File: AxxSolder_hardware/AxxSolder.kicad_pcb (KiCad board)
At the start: 2 copper layers, 39 x 82.5 mm, 138 parts, among them IC1 TLV76733DRVR, IC2 OPA2387DSGT, IC3 LMR54406DBVR, IC4 STM32G431CBT6, IC5 TPD4E1U06DBVR, IC6 STUSB4500QTR, IC7 MAX16171ATA_VY+T, IC8 LTC4440AHMS8E, IC9 INA281A5QDBVRQ1, J1 USB4110-GF-A, J2 691243110009, J3 TSW-102-07-T-S, J4 61300611821, J5 TSW-102-07-T-S, J6 TSW-102-07-T-S, Q1 STL9P3LLH6, Q2 STL10N3LLH5, Q3 2N7002NXAKR, U2 PEC11J-9215F-S0015, U3 BSC014N04LS

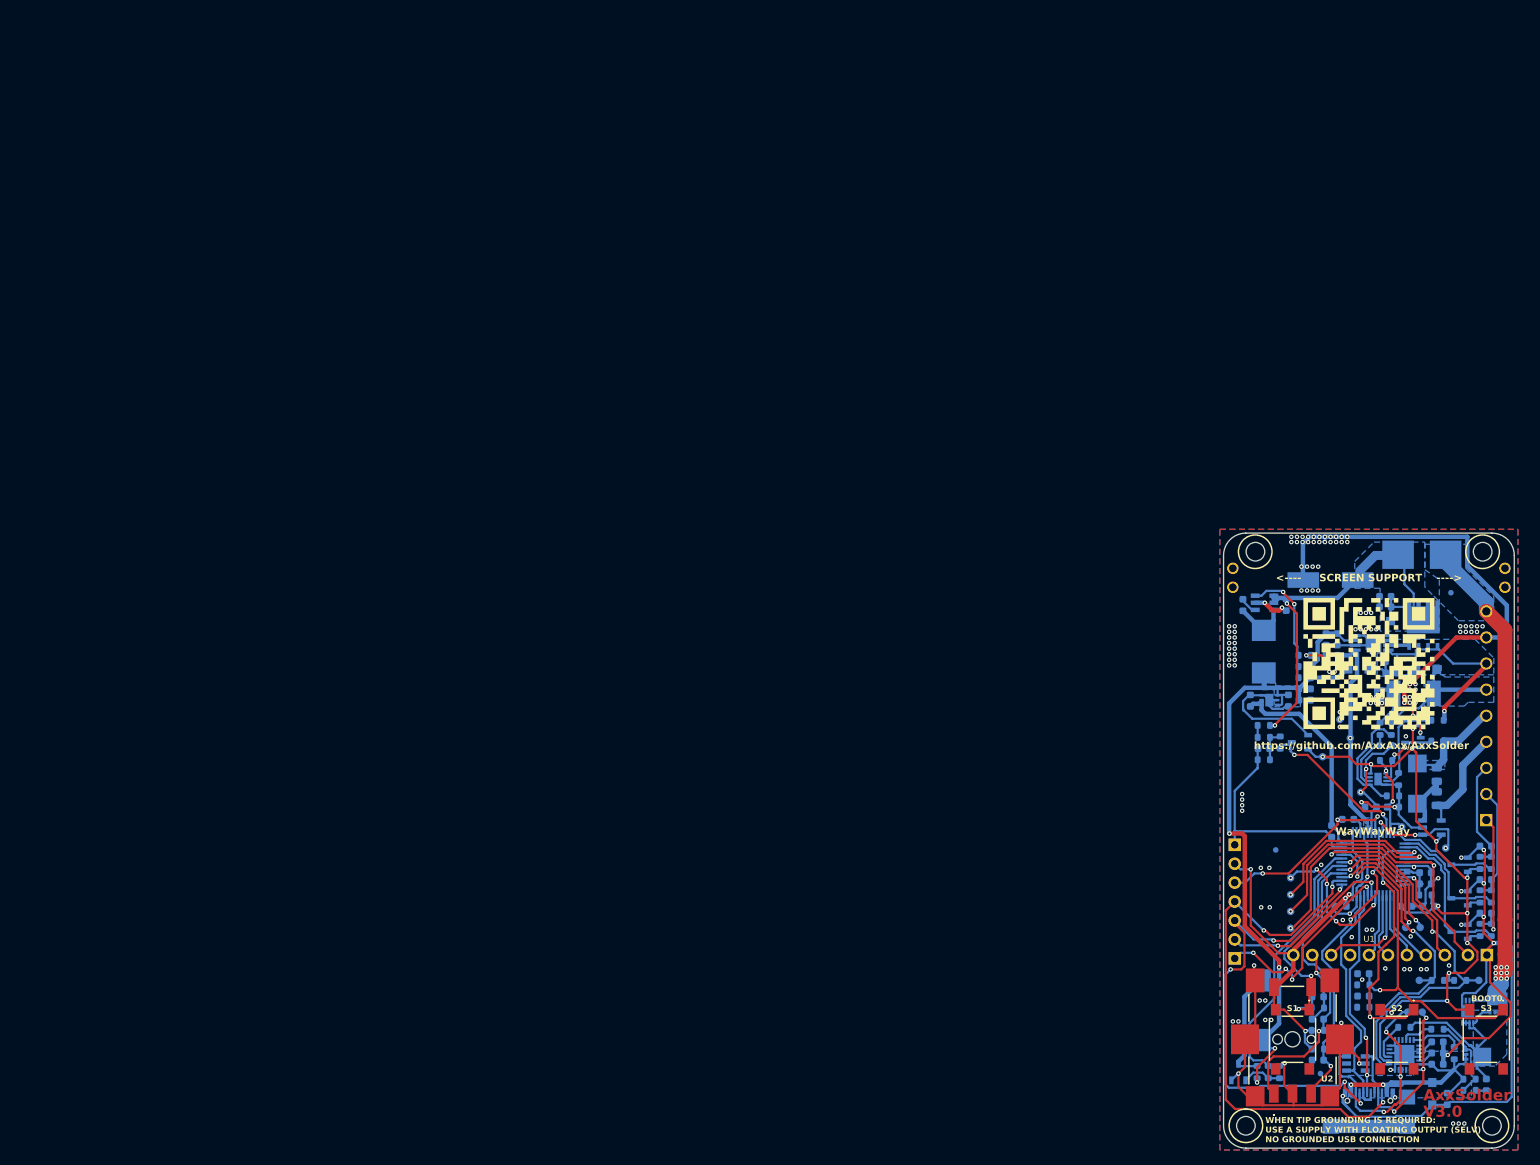
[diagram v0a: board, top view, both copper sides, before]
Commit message: Replace MCU with RP2040, new PCB layout
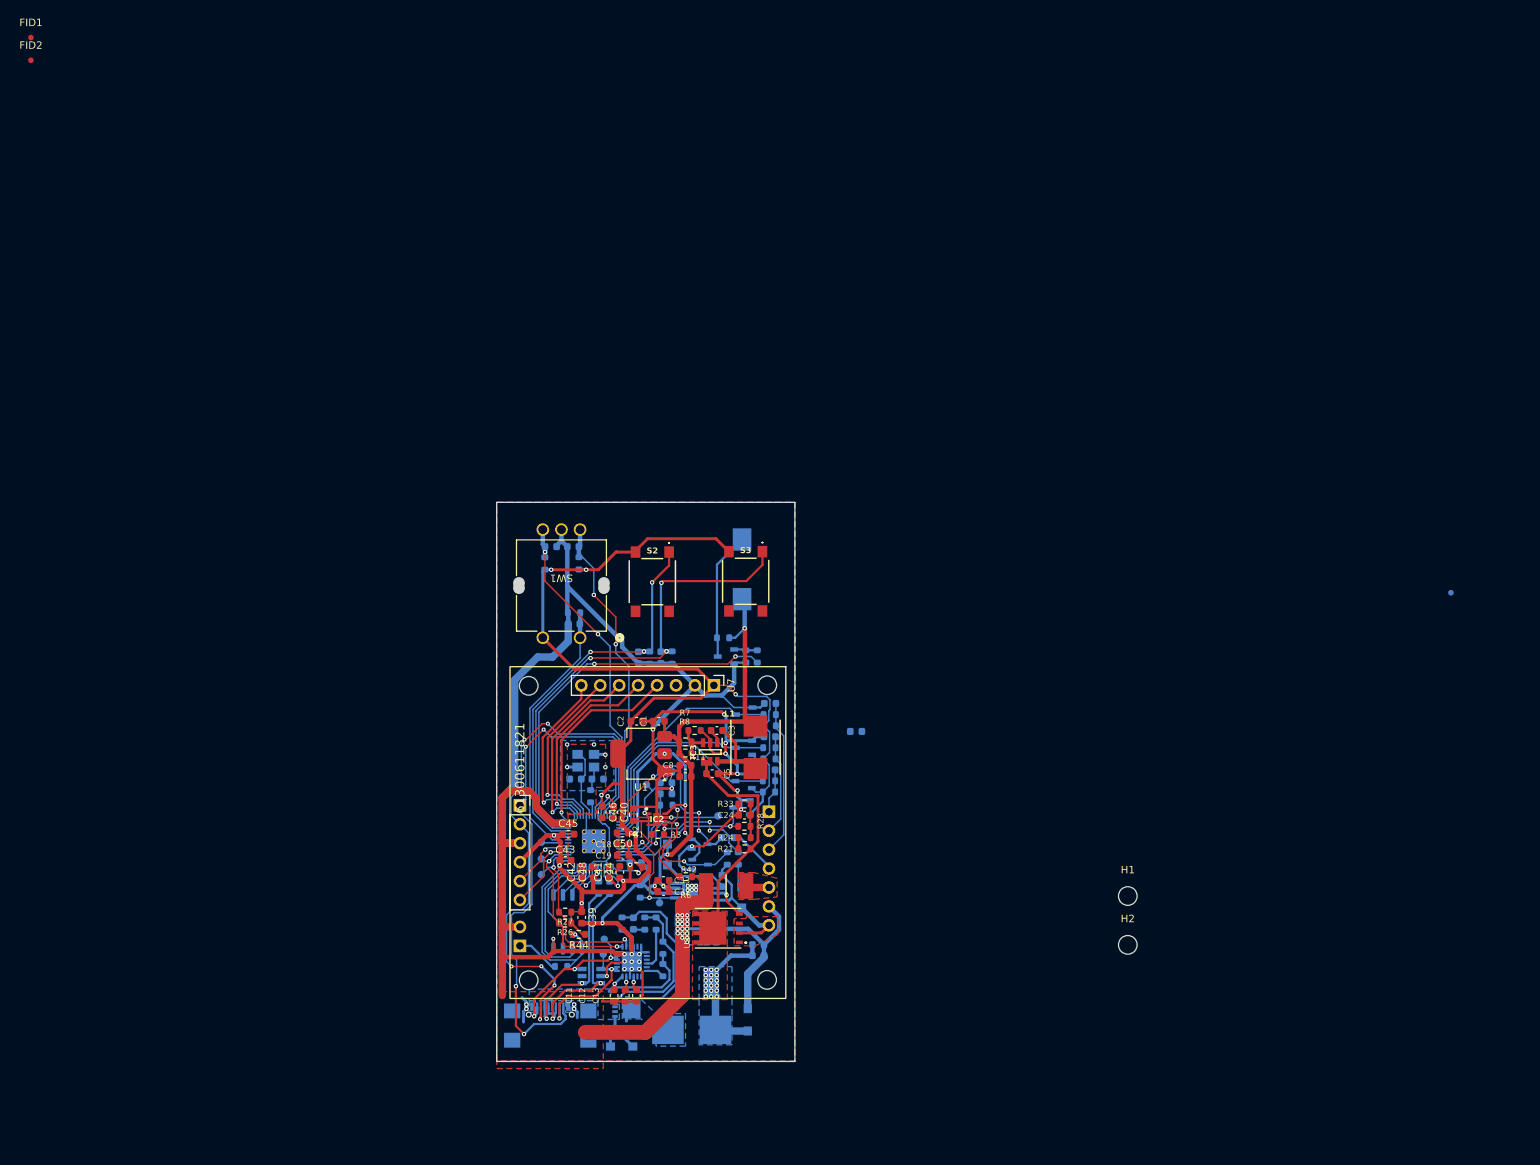
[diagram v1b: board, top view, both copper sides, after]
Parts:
- removed C14, C15, C16, C17: 100n, Capacitor_SMD:C_0603_1608Metric
- removed C31: 10u, Capacitor_SMD:C_0603_1608Metric
- removed F2: SF-2410FP100W-2, footprints:SF2410FP100W2
- removed G***: LOGO, LOGO
- removed IC1: TLV76733DRVR, footprints:SON65P200X200X80-7N
- removed IC4: STM32G431CBT6, footprints:QFP50P900X900X160-48N
- removed IC7: MAX16171ATA_VY+T, footprints:SON50P300X200X80-9N
- removed IC9: INA281A5QDBVRQ1, footprints:SOT95P280X145-5N
- removed J3: TSW-102-07-T-S, Connector_PinHeader_2.54mm:PinHeader_1x02_P2.54mm_Vertical
- removed J5, J6: TSW-102-07-T-S, footprints:TSW-102-XX-YY-S
- removed Q2: STL10N3LLH5, footprints:STL10N3LLH5
- removed S1: ADTSM644RVTR, footprints:ADTSM644RVTR
- removed TP1, TP14, TP2, TP5, TP6: DIAG_TP, TestPoint:TestPoint_Pad_D1.0mm
- removed TP12: GND_TP, TestPoint:TestPoint_Pad_D1.0mm
- removed TP13: DIAG_TP, Connector_PinSocket_2.54mm:PinSocket_1x01_P2.54mm_Vertical
- removed TP3: 3.3V_TP, TestPoint:TestPoint_Pad_D1.0mm
- removed TP9: Current_TP, TestPoint:TestPoint_Pad_D1.0mm
- removed U2: PEC11J-9215F-S0015, footprints:PEC11J9215FS0015
- added C36: 15p, Capacitor_SMD:C_0603_1608Metric, B.Cu at (74.1, 100.5)
- added C38: 15p, Capacitor_SMD:C_0603_1608Metric, B.Cu at (77.1, 100.5)
- added C39: 100n, Capacitor_SMD:C_0603_1608Metric, F.Cu at (74.9, 119.0)
- added C40: 100n, Capacitor_SMD:C_0603_1608Metric, F.Cu at (79.2, 104.9)
- added C41: 100n, Capacitor_SMD:C_0603_1608Metric, F.Cu at (78.5, 113.0)
- added C42: 1u, Capacitor_SMD:C_0603_1608Metric, F.Cu at (74.9, 113.0)
- added C43: 100n, Capacitor_SMD:C_0603_1608Metric, F.Cu at (72.7, 111.4)
- added C44: 1u, Capacitor_SMD:C_0603_1608Metric, F.Cu at (80.0, 113.0)
- added C45: 100n, Capacitor_SMD:C_0603_1608Metric, F.Cu at (73.1, 107.9)
- added C46: 100n, Capacitor_SMD:C_0603_1608Metric, F.Cu at (77.6, 104.9)
- added C47: 100n, Capacitor_SMD:C_0603_1608Metric, B.Cu at (82.1, 111.7)
- added C48: 100n, Capacitor_SMD:C_0603_1608Metric, F.Cu at (76.5, 113.0)
- added C50: 100n, Capacitor_SMD:C_0603_1608Metric, F.Cu at (80.4, 107.7)
- added H3: MountingHole, MountingHole:MountingHole_2.5mm, F.Cu at (67.8, 88.0)
- added H4: MountingHole, MountingHole:MountingHole_2.5mm, F.Cu at (99.8, 87.9)
- added H5: MountingHole, MountingHole:MountingHole_2.5mm, F.Cu at (67.8, 127.5)
- added H6: MountingHole, MountingHole:MountingHole_2.5mm, F.Cu at (99.8, 127.4)
- added J7: Conn_01x07_Pin, Connector_PinHeader_2.54mm:PinHeader_1x07_P2.54mm_Vertical, B.Cu at (100.0, 104.9)
- added R16: 1k, Resistor_SMD:R_0603_1608Metric, B.Cu at (76.1, 102.8)
- added R43: 1k, Resistor_SMD:R_0603_1608Metric, B.Cu at (72.1, 125.6)
- added R46: 27, Resistor_SMD:R_0603_1608Metric, B.Cu at (78.7, 115.1)
- added SW1: PEC11L-4220F-S0015, custom:PEC11L-4xxxF-Sxxxx_BRN, F.Cu at (74.7, 81.5)
- added U5: RP2040, custom:RP2040-QFN-56, B.Cu at (76.5, 108.8)
- added U6: W25Q128JVS, Package_SO:SOIC-8_5.23x5.23mm_P1.27mm, B.Cu at (73.0, 119.6)
- added U7: WS3-013992, custom:WS-13992, F.Cu at (92.6, 87.9)
- added Y1: ABM8-272-T3, Crystal:Crystal_SMD_3225-4Pin_3.2x2.5mm, B.Cu at (75.5, 98.0)
- C1, C11, C12, C13, C18, C19, C2, C24, C3, C32, C33, C5, C7, C8, FB1, FID1, FID2, IC2, IC3, J4, L1, R11, R2, R21, R24, R26, R27, R28, R3, R33, R42, R6, R7, R8, U3: moved to F.Cu
- J2: value 691243110009 -> Conn_01x02; footprint footprints:691243110009 -> Connector_PinHeader_2.54mm:PinHeader_1x02_P2.54mm_Vertical
- R44: value 1M -> 10k; footprint Resistor_SMD:R_0805_2012Metric -> Resistor_SMD:R_0603_1608Metric; moved to F.Cu
- R45: value 100m -> 27; footprint Resistor_SMD:R_0805_2012Metric -> Resistor_SMD:R_0603_1608Metric
- U1: value ~ -> LD1117S33TR_SOT223; footprint footprints:Adafruit_240x320_TFT -> Package_TO_SOT_SMD:SOT-223-3_TabPin2
- moved FID2 220.0 mm to (1.02, 4.08), turned to 0 degrees
- moved FID1 199.4 mm to (1.02, 1.02), turned to 0 degrees
- moved J2 130.7 mm to (66.6, 122.9), turned to 0 degrees
- moved TP16 126.6 mm to (69.5, 113.3), turned to 90 degrees
- moved C29 123.8 mm to (70.8, 69.3), turned to 0 degrees
- moved R36 122.4 mm to (70.0, 71.6), turned to 90 degrees
- moved R27 120.4 mm to (72.7, 118.3), turned to 0 degrees
- moved TP15 118.9 mm to (69.5, 111.2), turned to 90 degrees
- moved C28 118.3 mm to (73.7, 69.3)
- moved R26 117.3 mm to (72.7, 119.8)
- moved R35 117.3 mm to (74.5, 71.6), turned to 90 degrees
- moved S2 117.2 mm to (84.4, 74.0)
- moved R44 117.1 mm to (74.5, 121.3), turned to 180 degrees
- moved F1 116.9 mm to (89.7, 134.1)
- moved S3 116.8 mm to (96.9, 74.0)
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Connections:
- C9 pad 2: /VDD_IN_USBCPD -> /VDD_IN
- F1 pad 1: VDD -> /VDD_IN
- F1 pad 2: /VDD_IN -> VDD
- J2 pad 1: /S_sense -> /~{USB_BOOT}
- J2 pad 2: /H_sense2 -> GND
- J4 pad 1: GND -> /SWCLK
- J4 pad 2: +3.3V -> /SWDIO
- J4 pad 3: /NRST -> GND
- J4 pad 4: /SWCLK -> +3.3V
- J4 pad 5: /SWDIO -> /USART_RX
- Q1 pad 5: /VDD_IN_USBCPD -> /VDD_IN
- R17 pad 2: /VDD_IN_USBCPD -> /VDD_IN
- R35 pad 1: /ENC_B -> +3.3V
- R35 pad 2: +3.3V -> /ENC_B
- R44 pad 1: Net-(IC9-IN+) -> +3.3V
- R44 pad 2: /GREEN -> /QSPI_SS
- R45 pad 1: Earth -> /USB_D+
- R45 pad 2: Net-(IC9-IN+) -> Net-(U5-USB_DP)
- U1 pad 3: GND -> +7.5V
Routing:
- net GND: track 447.9 -> 381.2 mm, vias 149 -> 55
- net /VDD_IN: track 70.6 -> 23.6 mm, vias 9 -> 0
- net /USR4: track 46.0 -> 0.00 mm, vias 2 -> 0
- net +7.5V: track 95.8 -> 64.6 mm, vias 4 -> 3
- net /SDA: track 52.6 -> 24.7 mm
- net /NRST: track 26.5 -> 0.00 mm, vias 3 -> 0
- net +3.3V: track 200.1 -> 226.5 mm, vias 16 -> 14
- net /USR3: track 26.1 -> 0.00 mm, vias 2 -> 0
- net /QSPI_SS: track 0.00 -> 25.3 mm, vias 0 -> 1
- net +1V1: track 0.00 -> 24.4 mm, vias 0 -> 3
- net /USR2: track 23.1 -> 0.00 mm, vias 2 -> 0
- net /VDD_IN_USBCPD: track 22.7 -> 0.00 mm
- net /USART_RX: track 29.0 -> 8.85 mm, vias 4 -> 1
- net /SW3: track 46.9 -> 66.7 mm, vias 2 -> 3
- net /QSPI_SD1: track 0.00 -> 19.2 mm
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- added copper zone on F.Cu, net /BLUE
- added copper zone on F.Cu, net /RED
- added copper zone on F.Cu, net VDD
- removed copper zone on B.Cu, net +7.5V
- removed copper zone on B.Cu, net /BLUE
- removed copper zone on B.Cu, net /BOOST
- removed copper zone on B.Cu, net /GREEN
- removed copper zone on B.Cu, net /Heater
- removed copper zone on B.Cu, net /RED
- removed copper zone on B.Cu, net /VDD_IN_USBCPD
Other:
- board size 39 x 82.5 mm -> 40 x 75 mm
- board text removed: "2024-02"
- board text removed: "3.3V"
- board text removed: "9-24 VDC"
- board text removed: "<---- SCREEN SUPPORT ---->"
- board text removed: "AxxAxx"
- board text removed: "AxxSolder"
- board text removed: "BLU"
- board text removed: "BOOT0"
- board text removed: "C"
- board text removed: "GND"
- board text removed: "GRN"
- board text removed: "IN1"
- board text removed: "IN2"
- board text removed: "IO1"
- board text removed: "IO2"
- board text removed: "IO3"
- board text removed: "IO4"
- board text removed: "Input Voltage"
- board text removed: "NEVER SOLDER ON LIVE CIRCUITS!"
- board text removed: "NRST"
- board text removed: "PWM"
- board text removed: "RED"
- board text removed: "RX"
- board text removed: "SCL"
- board text removed: "SDA"
- board text removed: "STAND"
- board text removed: "STM32"
- board text removed: "STUSB4500"
- board text removed: "SWCLK"
- board text removed: "SWD"
- board text removed: "SWDIO"
- board text removed: "T"
- board text removed: "TX"
- board text removed: "USBC-PD"
- board text removed: "V3.0"
- board text removed: "VIN"
- board text removed: "WHEN TIP GROUNDING IS REQUIRED: USE A SUPPLY WITH FLOATING OUTPUT (SELV) NO GROUNDED USB CONNECTION"
- board text removed: "WayWayWay"
- board text removed: "https://github.com/AxxAxx/AxxSolder"

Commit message: Cleanup
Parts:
- removed H1, H2: MountingHole, MountingHole:MountingHole_2.5mm
- PWM: renamed from TP17; value SW_TP -> PWM
- moved FID2 166.4 mm to (101.6, 136.7)
- moved FID3 107.0 mm to (85.0, 65.3)
- moved R43 4.44 mm to (67.7, 125.4)
- moved C34 1.08 mm to (97.8, 123.5), turned to -90 degrees
- moved C35 1.01 mm to (99.3, 123.5), turned to -90 degrees
- moved U3 1.00 mm to (90.2, 121.5)
- renumbered TP7 to CC1, TP8 to CC2, TP10 to CURRENT, TP15 to SCL, TP16 to SDA, TP11 to TC
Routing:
- net GND: track 381.2 -> 375.7 mm, vias 55 -> 58
- net /~{USB_BOOT}: track 5.83 -> 2.64 mm
- net Net-(IC8-TG): track 6.19 -> 7.20 mm
- net /VBUS: track 20.5 -> 19.7 mm
- net /QSPI_SS: track 25.3 -> 25.8 mm
- net +1V1: track 24.4 -> 24.9 mm
- net /SWDIO: track 74.4 -> 73.9 mm
- net VDD: track 47.0 -> 47.2 mm, vias 18 -> 30

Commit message: Cleanup
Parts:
- removed C20: 10u, Capacitor_SMD:C_0603_1608Metric
- removed H3, H4, H5, H6: MountingHole, MountingHole:MountingHole_2.5mm
- removed J7: Conn_01x07_Pin, Connector_PinHeader_2.54mm:PinHeader_1x07_P2.54mm_Vertical
- removed SW1: PEC11L-4220F-S0015, custom:PEC11L-4xxxF-Sxxxx_BRN
- removed TP4: DIAG_TP, TestPoint:TestPoint_Pad_D1.0mm
- removed U7: WS3-013992, custom:WS-13992
- added C14: 100n, Capacitor_SMD:C_0603_1608Metric, F.Cu at (76.1, 94.7)
- added D11: 1_5inch-rgb-oled-module_asm-1110, custom_hmi:1_5inch-rgb-oled-module_asm-1110, F.Cu at (83.0, 114.0)
- added FID4: OSHW symbol, Symbol:OSHW-Logo_5.7x6mm_Copper, B.Cu at (80.8, 133.7)
- added FID5: Kicad symbol, Symbol:KiCad-Logo_6mm_SilkScreen, B.Cu at (88.2, 124.0)
- added J3: USB4105-GF-A, custom_connectors:GCT_USB4105-GF-A, F.Cu at (73.0, 62.7)
- added U2: PEC11L-4220F-S0015, custom_hmi:PEC11L4220FS0015, F.Cu at (71.6, 127.6)
- C10, C25, C26, C27, C4, C47, C6, C9, D1, D2, D3, D5, D6, D8, Q1, R1, R10, R12, R13, R14, R15, R17, R18, R19, R20, R22, R25, R29, R5, R9: moved to F.Cu
- C24, C3, C32, C33, C5, C7, C8, IC3, L1, R11, R21, R24, R26, R27, R28, R33, R42, R44, R7, R8, U3: moved to B.Cu
- J1: value USB4110-GF-A -> 284391-7; footprint footprints:USB4110GFA -> custom_connectors:CONN7_284391-7_TEC
- J4: footprint footprints:RHDR6W97P0X254_1X6_1574X250X865P -> Connector_PinHeader_2.54mm:PinHeader_1x06_P2.54mm_Vertical; moved to B.Cu
- TP10: renamed from CURRENT; value Current_TP -> Current
- TP11: renamed from TC; value TC_TP -> TC
- TP15: renamed from SCL; value DIAG_TP -> SCL
- TP16: renamed from SDA; value DIAG_TP -> SDA
- TP7: renamed from CC1; value DIAG_TP -> CC1
- TP8: renamed from CC2; value DIAG_TP -> CC2
- moved D3 74.3 mm to (66.7, 63.3), turned to 90 degrees
- moved FID3 70.4 mm to (85.2, 135.7)
- moved F1 68.9 mm to (84.0, 65.5)
- moved Q1 66.3 mm to (81.0, 65.1), turned to -90 degrees
- moved C28 63.3 mm to (69.9, 132.6), turned to 0 degrees
- moved C29 63.3 mm to (73.2, 132.6), turned to 180 degrees
- moved C10 63.0 mm to (74.0, 71.7), turned to 90 degrees
- moved D4 61.4 mm to (94.3, 71.5), turned to 0 degrees
- moved R35 59.7 mm to (69.9, 131.1), turned to 180 degrees
- moved R36 59.6 mm to (73.2, 131.1), turned to 0 degrees
- moved C37 58.9 mm to (96.7, 65.5), turned to 0 degrees
- moved C11 58.4 mm to (77.5, 71.2), turned to 0 degrees
- moved LS1 58.3 mm to (96.6, 130.4)
- moved C12 57.0 mm to (77.5, 72.7), turned to 0 degrees
- moved C13 55.6 mm to (77.5, 74.2), turned to 0 degrees
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- renumbered PWM to TP17
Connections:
- C28 pad 1: /ENC_B -> /ENC_A
- C29 pad 1: /ENC_A -> /ENC_B
- IC5 pad 3: /USB_D- -> /USB_D+
- IC5 pad 4: /USB_D+ -> /USB_D-
- R35 pad 2: /ENC_B -> /ENC_A
- R36 pad 2: /ENC_A -> /ENC_B
- U5 pad 11: /SW2 -> unconnected-(U5-GPIO8-Pad11)
- U5 pad 12: /SW3 -> /SW1
- U5 pad 13: /Buzzer -> /ENC_A
- U5 pad 14: /SPI_MOSI -> /SPI_RST
- U5 pad 15: /SPI_CS -> /SPI_DC
- U5 pad 16: /SPI_SCK -> /SPI_CS
- U5 pad 17: /SPI_RST -> /SPI_SCK
- U5 pad 18: /SPI_DC -> /SPI_MOSI
- U5 pad 28: /ENC_A -> /USART_RX
- U5 pad 29: /ENC_B -> /USART_TX
- U5 pad 4: /USART_TX -> /Buzzer
- U5 pad 5: /USART_RX -> /SW3
- U5 pad 6: /USR1 -> /SW2
- U5 pad 8: unconnected-(U5-GPIO6-Pad8) -> /ENC_B
- U5 pad 9: /SW1 -> unconnected-(U5-GPIO7-Pad9)
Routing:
- net GND: track 375.7 -> 275.1 mm, vias 58 -> 67
- net +7.5V: track 64.6 -> 114.7 mm
- net (no net): track 0.00 -> 49.7 mm
- net /SDA: track 24.7 -> 54.6 mm
- net /SCL: track 24.3 -> 53.7 mm
- net /SW3: track 66.6 -> 37.4 mm, vias 3 -> 2
- net /SW2: track 53.7 -> 26.2 mm, vias 3 -> 2
- net /SWDIO: track 73.9 -> 46.9 mm, vias 6 -> 1
- net +3.3V: track 226.2 -> 202.1 mm, vias 14 -> 15
- net VDD: track 47.2 -> 24.9 mm, vias 30 -> 0
- net /Buzzer: track 50.5 -> 29.7 mm
- net /SWCLK: track 74.9 -> 54.4 mm, vias 4 -> 1
- net /VDD_IN: track 23.6 -> 4.61 mm, vias 0 -> 16
- net /USB_D+: track 26.2 -> 43.7 mm
- net Net-(Q1-G): track 20.1 -> 5.31 mm
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- added copper zone on B.Cu, net +1V1
- added copper zone on B.Cu, net +3.3V
- added copper zone on B.Cu, net /BLUE
- added copper zone on B.Cu, net /RED
- added copper zone on F.Cu, net /VBUS
- removed copper zone on F.Cu, net /BLUE
- removed copper zone on F.Cu, net /RED
- removed copper zone on B.Cu, net /VBUS
- removed copper zone on B.Cu, net /VDD_IN
- removed copper zone on F.Cu, net VDD
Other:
- board size 40 x 75 mm -> 40 x 78.3 mm

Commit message: Cleanup
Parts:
- added FID6: Fiducial, Fiducial:Fiducial_0.75mm_Mask1.5mm, B.Cu at (65.4, 66.8)
- moved FID1 92.1 mm to (65.4, 66.8)
- moved C7 3.21 mm to (68.2, 83.3), turned to 90 degrees
- moved C3 3.11 mm to (73.0, 79.2), turned to -90 degrees
- moved C8 1.80 mm to (68.2, 80.3), turned to -90 degrees
- moved L1 1.55 mm to (73.5, 84.5)
- moved R11 1.45 mm to (73.1, 76.3), turned to -90 degrees
- moved R7 1.22 mm to (70.8, 80.0)
- moved R8 1.20 mm to (70.8, 78.5)
- moved R4 1.20 mm to (89.2, 89.5)
- moved C40 0.90 mm to (83.0, 105.3), turned to -90 degrees
- moved C5 0.80 mm to (76.3, 76.4)
- moved D7 0.77 mm to (72.0, 90.8)
- moved R28 0.77 mm to (75.3, 89.7)
- moved R33 0.77 mm to (75.3, 91.2)
- moved C24 0.15 mm to (78.2, 91.9)
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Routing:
- net GND: track 275.1 -> 264.1 mm, vias 67 -> 72
- net (no net): track 49.7 -> 52.9 mm
- net +3.3V: track 202.1 -> 204.8 mm, vias 15 -> 18
- net +7.5V: track 114.7 -> 116.9 mm
- net Net-(IC3-SW): track 6.71 -> 4.68 mm
- net Net-(IC2B-+): track 13.9 -> 15.1 mm
- net /CC1: track 13.9 -> 13.2 mm
- net /QSPI_SS: track 19.6 -> 19.0 mm
- net /QSPI_SD1: track 14.0 -> 13.3 mm
- net Net-(IC3-CB): track 1.70 -> 2.36 mm
- net VDD: track 24.9 -> 24.3 mm
- added copper zone on F.Cu, net +3.3V
- added copper zone on B.Cu, net +7.5V
- added copper zone on B.Cu, net Net-(IC3-SW)

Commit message: Ready?
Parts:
- C10, C11, C12, C13, R14: moved to B.Cu
- IC5, TP7, TP8: moved to F.Cu
- moved TP7 7.03 mm to (77.7, 72.7)
- moved TP8 6.56 mm to (75.6, 70.8)
- moved C10 1.93 mm to (72.3, 70.9), turned to 0 degrees
- moved IC5 1.68 mm to (71.5, 72.1), turned to -90 degrees
- moved C11 1.65 mm to (76.0, 70.3), turned to 180 degrees
- moved R14 1.64 mm to (76.0, 74.8)
- moved C12 1.62 mm to (76.1, 71.8), turned to 180 degrees
- moved C13 1.60 mm to (76.1, 73.3), turned to 180 degrees
- moved R11 1.06 mm to (72.3, 77.0), turned to 0 degrees
- moved Q1 0.06 mm to (81.0, 65.0)
- moved C9 0.06 mm to (84.8, 68.8)
- moved R12 0.06 mm to (80.3, 68.8)
- moved R13 0.06 mm to (83.3, 68.8)
- moved R15 0.06 mm to (81.8, 68.8)
- moved R17 0.06 mm to (86.3, 68.8)
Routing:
- net GND: track 264.1 -> 254.7 mm, vias 72 -> 79
- net /CC2: track 17.9 -> 20.7 mm, vias 3 -> 1
- net /USB_D-: track 40.8 -> 43.4 mm, vias 2 -> 3
- net /SWDIO: track 46.9 -> 48.9 mm, vias 1 -> 3
- net Net-(IC6-VBUS_VS_DISCH): track 1.17 -> 2.35 mm, vias 1 -> 0
- net (no net): track 52.9 -> 52.0 mm
- net Net-(IC6-VREG_1V2): track 2.21 -> 1.48 mm, vias 1 -> 0
- net /USB_D+: track 43.7 -> 44.4 mm, vias 2 -> 3
- net Net-(IC6-VREG_2V7): track 2.07 -> 1.43 mm, vias 1 -> 0
- net /VDD_IN: track 4.61 -> 4.87 mm, vias 16 -> 24
- net /CC1: track 13.2 -> 13.4 mm, vias 2 -> 3
- net /VBUS: track 22.4 -> 22.5 mm, vias 3 -> 2
- added copper zone on B.Cu, net /VDD_IN
- added copper zone on F.Cu, net /VDD_IN
